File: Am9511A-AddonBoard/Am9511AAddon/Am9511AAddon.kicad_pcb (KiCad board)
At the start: 2 copper layers, 72 x 47 mm, 16 parts, among them J1 Conn_02x12, J2 Conn_01x02, U1 MCP810, U2 74HCT573, U3 74HCT574, U4 74HCT00, U5 APU Clock, U6 Am9511A-1DC

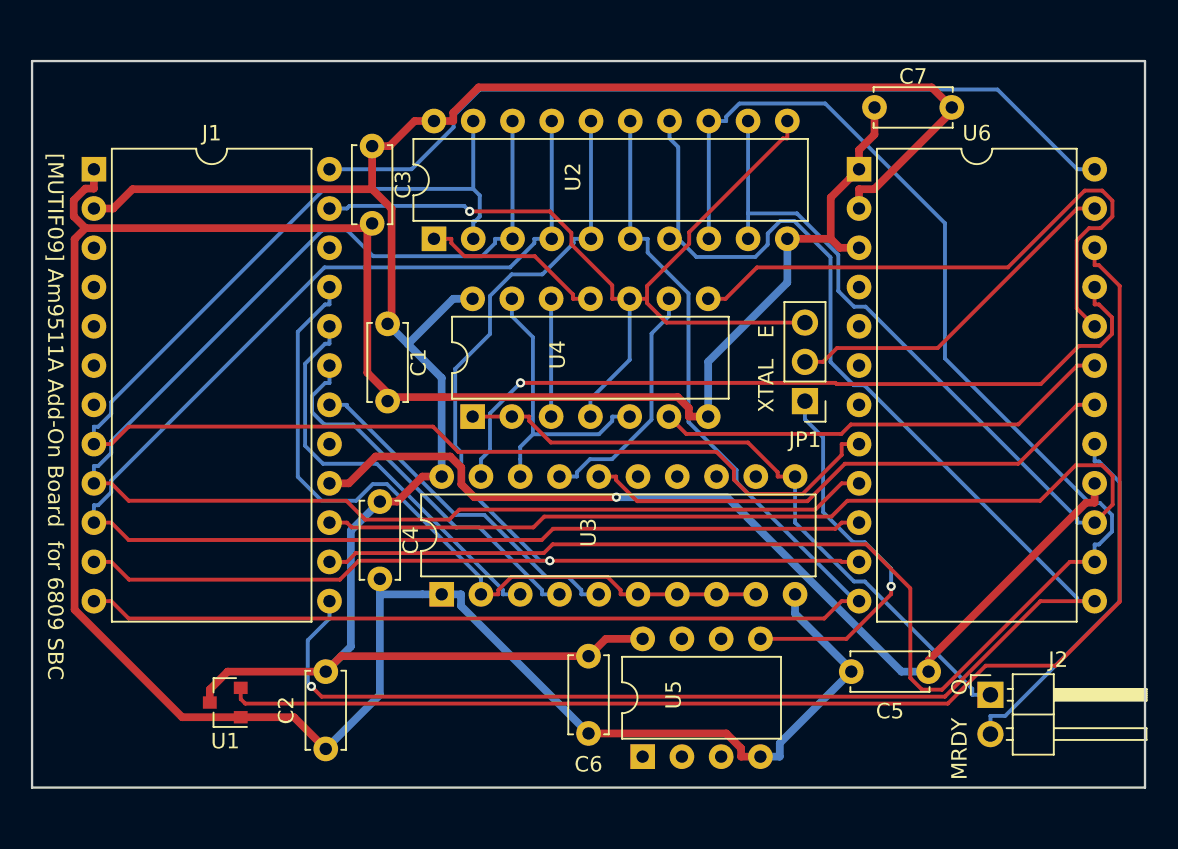
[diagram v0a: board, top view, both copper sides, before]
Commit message: Update design materials of Am9511A Add-on board (now, Rev.2)
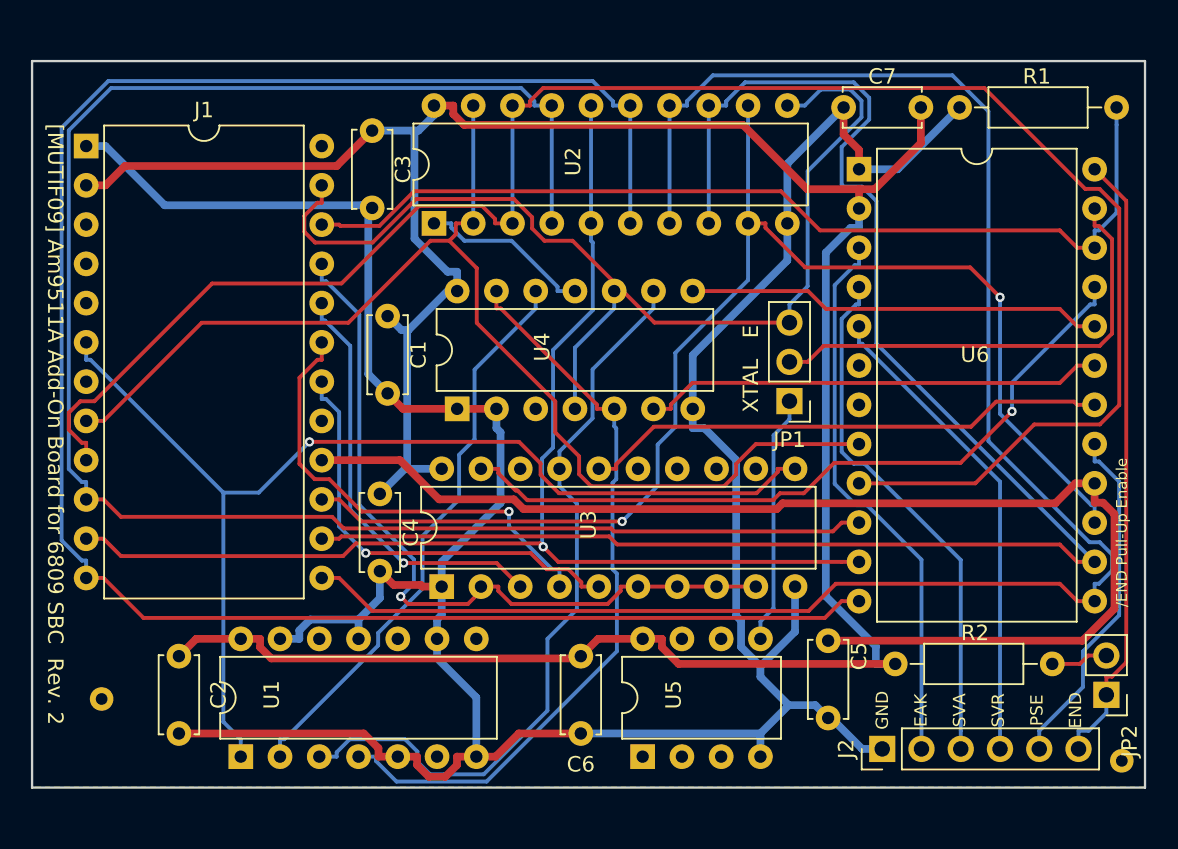
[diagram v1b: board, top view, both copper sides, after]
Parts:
- added ?: via, sbclib:via, F.Cu at (120.5, 74.0)
- added ?: via, sbclib:via, F.Cu at (54.5, 70.0)
- added JP2: Pullup_Enable, Pin_Headers:Pin_Header_Straight_1x02_Pitch2.54mm, F.Cu at (119.5, 71.0)
- added R1: 10k, Resistors_THT:R_Axial_DIN0207_L6.3mm_D2.5mm_P10.16mm_Horizontal, F.Cu at (110.0, 33.0)
- added R2: 10k, Resistors_THT:R_Axial_DIN0207_L6.3mm_D2.5mm_P10.16mm_Horizontal, F.Cu at (116.0, 69.0)
- J2: value Conn_01x02 -> Conn_01x06; footprint Pin_Headers:Pin_Header_Angled_1x02_Pitch2.54mm -> Pin_Headers:Pin_Header_Straight_1x06_Pitch2.54mm
- JP1: value Clock Sel -> Clock Selection
- U1: value MCP810 -> 74HCT04; footprint TO_SOT_Packages_SMD:SOT-23 -> Housings_DIP:DIP-14_W7.62mm
- U5: value APU Clock -> XTAL OSC 3.0 MHz
- moved C2 11.2 mm to (59.5, 68.5), turned to 270 degrees
- moved J2 7.83 mm to (105.0, 74.5), turned to 90 degrees
- moved C5 6.80 mm to (101.5, 67.5), turned to 270 degrees
- moved U1 3.64 mm to (63.5, 75.0), turned to 90 degrees
- moved C7 2.00 mm to (102.5, 33.0)
- moved J1 1.58 mm to (53.5, 35.5)
- moved U4 1.12 mm to (77.5, 52.5)
- moved C3 1.00 mm to (72.0, 34.5)
- moved JP1 1.00 mm to (99.0, 52.0)
- moved U2 1.00 mm to (76.0, 40.5)
- moved C1 0.50 mm to (73.0, 46.5)
- moved C4 0.50 mm to (72.5, 58.0)
- moved C6 0.50 mm to (85.5, 68.5)
- moved U3 0.50 mm to (76.5, 64.0)
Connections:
- C2 pad 1: GND -> VCC
- C2 pad 2: VCC -> GND
- J1 pad 24: //END -> Net-(J1-Pad24)
- J1 pad 6: Net-(J1-Pad6) -> /Q
- J2 pad 1: /Q -> GND
- J2 pad 2: /MRDY -> Net-(J2-Pad2)
- U1 pad 1: GND -> /Q
- U1 pad 3: VCC -> Net-(U1-Pad3)
- U3 pad 17: Net-(U3-Pad17) -> Net-(U1-Pad3)
- U4 pad 1: /Q -> GND
- U4 pad 12: Net-(U4-Pad12) -> Net-(U1-Pad2)
- U4 pad 13: Net-(U3-Pad18) -> Net-(U1-Pad4)
- U4 pad 2: /Q -> GND
- U4 pad 3: Net-(U4-Pad12) -> Net-(U4-Pad3)
- U4 pad 5: Net-(U3-Pad18) -> Net-(U1-Pad4)
- U4 pad 9: Net-(U3-Pad17) -> Net-(U1-Pad3)
- U6 pad 17: /MRDY -> //PAUSE
- U6 pad 22: Net-(U1-Pad2) -> Net-(J1-Pad22)
- U6 pad 3: GND -> Net-(J2-Pad2)
- U6 pad 4: Net-(U6-Pad4) -> Net-(J2-Pad3)
- U6 pad 5: Net-(U6-Pad5) -> Net-(J2-Pad4)
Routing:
- net Net-(J1-Pad22): track 0.00 -> 62.3 mm
- net Net-(U1-Pad3): track 0.00 -> 49.3 mm
- net Net-(U1-Pad4): track 0.00 -> 48.6 mm
- net Net-(U1-Pad2): track 84.2 -> 37.1 mm
- net /DB4: track 88.4 -> 128.0 mm
- net Net-(J2-Pad2): track 0.00 -> 36.0 mm
- net Net-(J2-Pad3): track 0.00 -> 34.1 mm
- net VCC: track 144.2 -> 178.0 mm
- net Net-(J2-Pad4): track 0.00 -> 31.2 mm
- net /Q: track 43.3 -> 72.0 mm, vias 0 -> 1
- net /DB1: track 95.3 -> 121.0 mm
- net /MRDY: track 23.6 -> 0.00 mm
- net //PAUSE: track 0.00 -> 22.7 mm
- net /DB2: track 96.5 -> 116.2 mm
- net Net-(U3-Pad18): track 19.3 -> 0.00 mm
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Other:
- board text added: "/END Pull-Up Enable"
- board text added: "EAK"
- board text added: "END"
- board text added: "GND"
- board text added: "PSE"
- board text added: "SVA"
- board text added: "SVR"
- board text added: "[MUTIF09] Am9511A Add-On Board for 6809 SBC Rev. 2"
- board text removed: "MRDY"
- board text removed: "Q"
- board text removed: "[MUTIF09] Am9511A Add-On Board for 6809 SBC"
